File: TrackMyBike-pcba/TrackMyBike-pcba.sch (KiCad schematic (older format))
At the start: 3 parts

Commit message: Add project description
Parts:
- gave numbers to parts that had none: 1
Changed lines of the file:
@@
 $EndSheet
 $Comp
-L Connector_Generic:Conn_01x02 J?
+L Connector_Generic:Conn_01x02 J
 U 1 1 5F18731B
 P 8900 1150
-F 0 "J?" H 8980 1142 50  0000 L CNN
+F 0 "J" H 8980 1142 50  0000 L CNN
 F 1 "Conn_01x02" H 8980 1051 50  0000 L CNN
 F 2 "" H 8900 1150 50  0001 C CNN
@@
 $EndComp
 $Comp
-L Connector_Generic:Conn_01x02 J?
+L Connector_Generic:Conn_01x02 J
 U 1 1 5F187BB9
 P 10350 1150
-F 0 "J?" H 10430 1142 50  0000 L CNN
+F 0 "J" H 10430 1142 50  0000 L CNN
 F 1 "Conn_01x02" H 10430 1051 50  0000 L CNN
 F 2 "" H 10350 1150 50  0001 C CNN
@@
 $EndComp
 $Comp
-L power:+BATT #PWR?
+L power:+BATT #PWR
 U 1 1 5F1880E1
 P 8700 1150
-F 0 "#PWR?" H 8700 1000 50  0001 C CNN
+F 0 "#PWR" H 8700 1000 50  0001 C CNN
 F 1 "+BATT" H 8715 1323 50  0000 C CNN
 F 2 "" H 8700 1150 50  0001 C CNN
@@
 $EndComp
 $Comp
-L power:GND #PWR?
+L power:GND #PWR
 U 1 1 5F188BA8
 P 8700 1250
-F 0 "#PWR?" H 8700 1000 50  0001 C CNN
+F 0 "#PWR" H 8700 1000 50  0001 C CNN
 F 1 "GND" H 8705 1077 50  0000 C CNN
 F 2 "" H 8700 1250 50  0001 C CNN
@@
 $EndComp
 $Comp
-L power:GND #PWR?
+L power:GND #PWR
 U 1 1 5F188E4C
 P 10150 1250
-F 0 "#PWR?" H 10150 1000 50  0001 C CNN
+F 0 "#PWR" H 10150 1000 50  0001 C CNN
 F 1 "GND" H 10155 1077 50  0000 C CNN
 F 2 "" H 10150 1250 50  0001 C CNN
@@
 $EndComp
 $Comp
-L power:VSOLAR #PWR?
+L power:VSOLAR #PWR
 U 1 1 5F18A31C
 P 10150 1150
-F 0 "#PWR?" H 10150 1000 50  0001 C CNN
+F 0 "#PWR" H 10150 1000 50  0001 C CNN
 F 1 "VSOLAR" H 10165 1323 50  0000 C CNN
 F 2 "" H 10150 1150 50  0001 C CNN
@@
 $EndSheet
 $Comp
-L Connector:USB_B_Micro J?
+L Connector:USB_B_Micro J
 U 1 1 5F19E94A
 P 8850 2100
-F 0 "J?" H 8907 2567 50  0000 C CNN
+F 0 "J" H 8907 2567 50  0000 C CNN
 F 1 "USB_B_Micro" H 8907 2476 50  0000 C CNN
 F 2 "" H 9000 2050 50  0001 C CNN
@@
 NoConn ~ 9150 2300
 $Comp
-L power:GND #PWR?
+L power:GND #PWR
 U 1 1 5F19E955
 P 8750 2600
-F 0 "#PWR?" H 8750 2350 50  0001 C CNN
+F 0 "#PWR" H 8750 2350 50  0001 C CNN
 F 1 "GND" H 8755 2427 50  0000 C CNN
 F 2 "" H 8750 2600 50  0001 C CNN
@@
 	8750 2550 8750 2600
 $Comp
-L power:VBUS #PWR?
+L power:VBUS #PWR
 U 1 1 5F19EF28
 P 9400 1900
-F 0 "#PWR?" H 9400 1750 50  0001 C CNN
+F 0 "#PWR" H 9400 1750 50  0001 C CNN
 F 1 "VBUS" H 9415 2073 50  0000 C CNN
 F 2 "" H 9400 1900 50  0001 C CNN

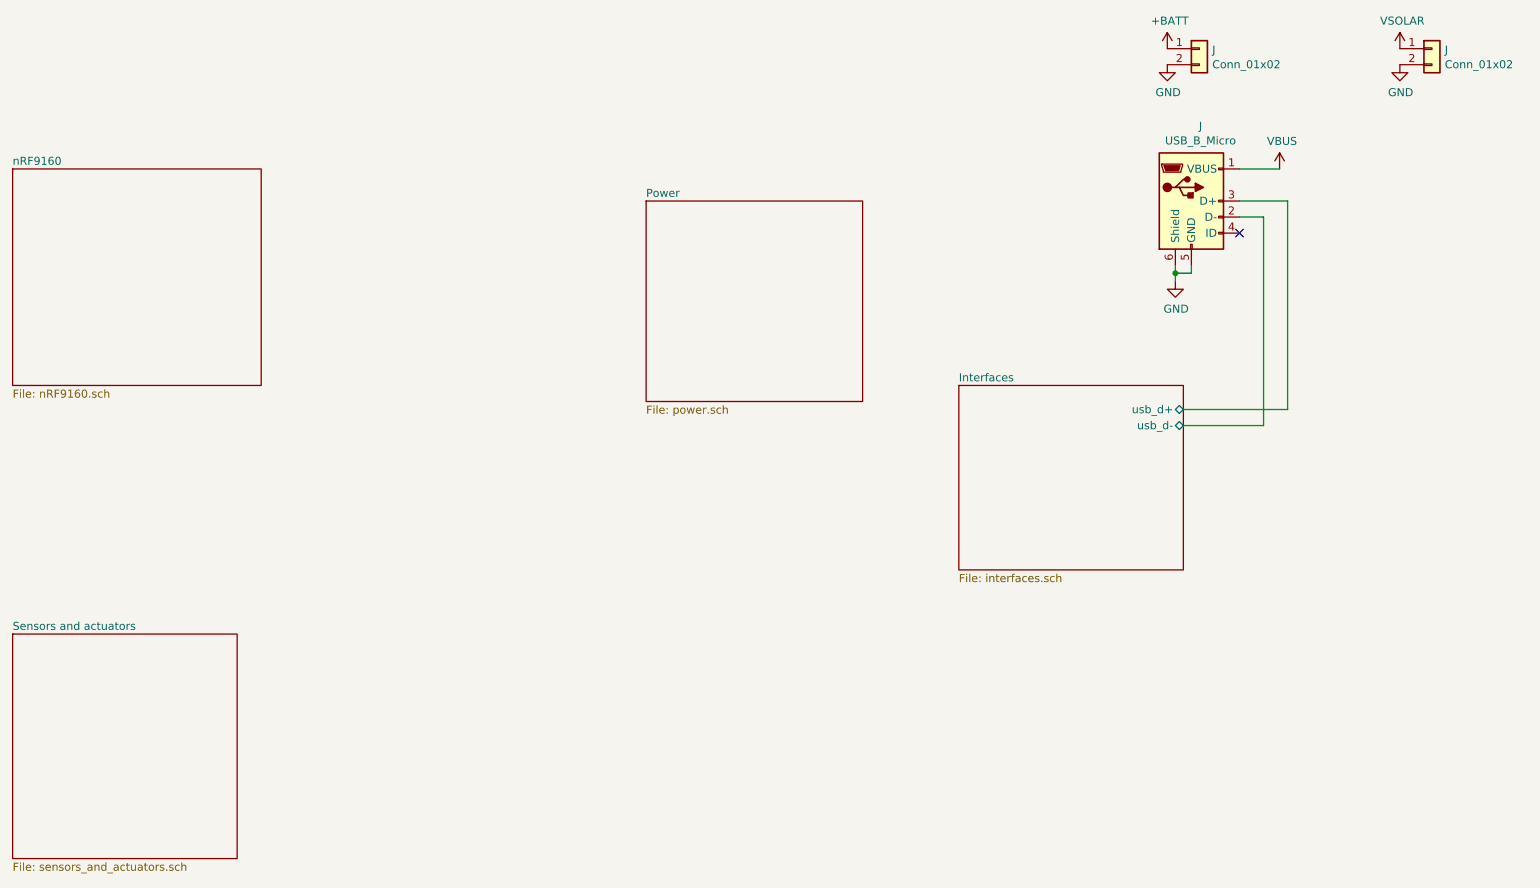
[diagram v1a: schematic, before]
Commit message: Add SIM card, FTDI IC
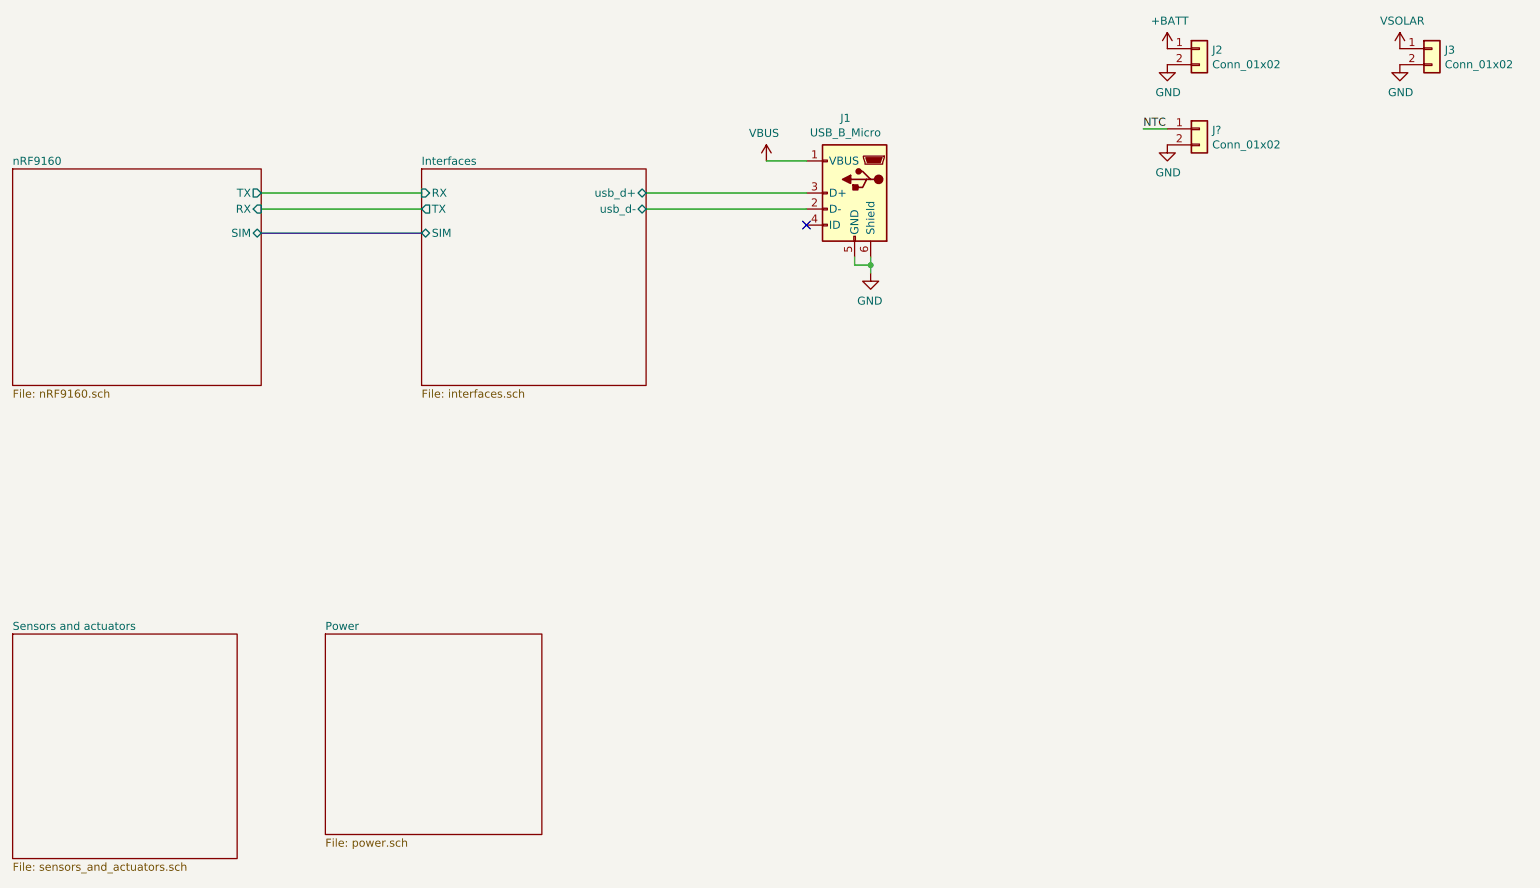
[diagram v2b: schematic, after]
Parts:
- added J?: Conn_01x02, symbol Connector_Generic:Conn_01x02
- renumbered J to J1, J to J2, J to J3
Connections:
- net GND: now also J?.2 (Pin_2)
- new net NTC: J?.1 (Pin_1)
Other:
- moved on the sheet: J1
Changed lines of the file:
@@
 F0 "nRF9160" 50
 F1 "nRF9160.sch" 50
+F2 "SIM" B R 3050 2300 50
+F3 "RX" I R 3050 2150 50
+F4 "TX" O R 3050 2050 50
 $EndSheet
 $Sheet
-S 5450 2100 1350 1250
+S 3450 4800 1350 1250
 U 5F16A6AE
 F0 "Power" 50
 F1 "power.sch" 50
 $EndSheet
+$Sheet
+S 1500 4800 1400 1400
+U 5F18B9BE
+F0 "Sensors and actuators" 50
+F1 "sensors_and_actuators.sch" 50
+$EndSheet
+$Sheet
+S 4050 1900 1400 1350
+U 5F19B71B
+F0 "Interfaces" 50
+F1 "interfaces.sch" 50
+F2 "usb_d+" B R 5450 2050 50
+F3 "usb_d-" B R 5450 2150 50
+F4 "RX" I L 4050 2050 50
+F5 "TX" O L 4050 2150 50
+F6 "SIM" B L 4050 2300 50
+$EndSheet
 $Comp
-L Connector_Generic:Conn_01x02 J
-U 1 1 5F18731B
-P 8900 1150
-F 0 "J" H 8980 1142 50  0000 L CNN
-F 1 "Conn_01x02" H 8980 1051 50  0000 L CNN
-F 2 "" H 8900 1150 50  0001 C CNN
-F 3 "~" H 8900 1150 50  0001 C CNN
-	1    8900 1150
+L power:VSOLAR #PWR0101
+U 1 1 5F18A31C
+P 10150 1150
+F 0 "#PWR0101" H 10150 1000 50  0001 C CNN
+F 1 "VSOLAR" H 10165 1323 50  0000 C CNN
+F 2 "" H 10150 1150 50  0001 C CNN
+F 3 "" H 10150 1150 50  0001 C CNN
+	1    10150 1150
 	1    0    0    -1
 $EndComp
 $Comp
-L Connector_Generic:Conn_01x02 J
+L power:GND #PWR0102
+U 1 1 5F188E4C
+P 10150 1250
+F 0 "#PWR0102" H 10150 1000 50  0001 C CNN
+F 1 "GND" H 10155 1077 50  0000 C CNN
+F 2 "" H 10150 1250 50  0001 C CNN
+F 3 "" H 10150 1250 50  0001 C CNN
+	1    10150 1250
+	1    0    0    -1
+$EndComp
+$Comp
+L power:GND #PWR0103
+U 1 1 5F188BA8
+P 8700 1250
+F 0 "#PWR0103" H 8700 1000 50  0001 C CNN
+F 1 "GND" H 8705 1077 50  0000 C CNN
+F 2 "" H 8700 1250 50  0001 C CNN
+F 3 "" H 8700 1250 50  0001 C CNN
+	1    8700 1250
+	1    0    0    -1
+$EndComp
+$Comp
+L power:+BATT #PWR0104
+U 1 1 5F1880E1
+P 8700 1150
+F 0 "#PWR0104" H 8700 1000 50  0001 C CNN
+F 1 "+BATT" H 8715 1323 50  0000 C CNN
+F 2 "" H 8700 1150 50  0001 C CNN
+F 3 "" H 8700 1150 50  0001 C CNN
+	1    8700 1150
+	1    0    0    -1
+$EndComp
+$Comp
+L Connector_Generic:Conn_01x02 J3
 U 1 1 5F187BB9
 P 10350 1150
-F 0 "J" H 10430 1142 50  0000 L CNN
+F 0 "J3" H 10430 1142 50  0000 L CNN
 F 1 "Conn_01x02" H 10430 1051 50  0000 L CNN
 F 2 "" H 10350 1150 50  0001 C CNN
@@
 $EndComp
 $Comp
-L power:+BATT #PWR
-U 1 1 5F1880E1
-P 8700 1150
-F 0 "#PWR" H 8700 1000 50  0001 C CNN
-F 1 "+BATT" H 8715 1323 50  0000 C CNN
-F 2 "" H 8700 1150 50  0001 C CNN
-F 3 "" H 8700 1150 50  0001 C CNN
-	1    8700 1150
+L Connector_Generic:Conn_01x02 J2
+U 1 1 5F18731B
+P 8900 1150
+F 0 "J2" H 8980 1142 50  0000 L CNN
+F 1 "Conn_01x02" H 8980 1051 50  0000 L CNN
+F 2 "" H 8900 1150 50  0001 C CNN
+F 3 "~" H 8900 1150 50  0001 C CNN
+	1    8900 1150
+	1    0    0    -1
+$EndComp
+Wire Wire Line
+	5450 2150 6450 2150
+Wire Wire Line
+	5450 2050 6450 2050
+Wire Wire Line
+	6450 1850 6200 1850
+$Comp
+L power:VBUS #PWR0105
+U 1 1 5F19EF28
+P 6200 1850
+F 0 "#PWR0105" H 6200 1700 50  0001 C CNN
+F 1 "VBUS" H 6215 2023 50  0000 C CNN
+F 2 "" H 6200 1850 50  0001 C CNN
+F 3 "" H 6200 1850 50  0001 C CNN
+	1    6200 1850
+	-1   0    0    -1
+$EndComp
+Wire Wire Line
+	6850 2500 6850 2550
+Connection ~ 6850 2500
+Wire Wire Line
+	6750 2500 6750 2450
+Wire Wire Line
+	6850 2500 6750 2500
+Wire Wire Line
+	6850 2450 6850 2500
+$Comp
+L power:GND #PWR0106
+U 1 1 5F19E955
+P 6850 2550
+F 0 "#PWR0106" H 6850 2300 50  0001 C CNN
+F 1 "GND" H 6855 2377 50  0000 C CNN
+F 2 "" H 6850 2550 50  0001 C CNN
+F 3 "" H 6850 2550 50  0001 C CNN
+	1    6850 2550
+	-1   0    0    -1
+$EndComp
+NoConn ~ 6450 2250
+$Comp
+L Connector:USB_B_Micro J1
+U 1 1 5F19E94A
+P 6750 2050
+F 0 "J1" H 6807 2517 50  0000 C CNN
+F 1 "USB_B_Micro" H 6807 2426 50  0000 C CNN
+F 2 "" H 6900 2000 50  0001 C CNN
+F 3 "~" H 6900 2000 50  0001 C CNN
+	1    6750 2050
+	-1   0    0    -1
+$EndComp
+Wire Bus Line
+	3050 2300 4050 2300
+Wire Wire Line
+	3050 2150 4050 2150
+Wire Wire Line
+	4050 2050 3050 2050
+$Comp
+L power:GND #PWR?
+U 1 1 5F1C3374
+P 8700 1750
+F 0 "#PWR?" H 8700 1500 50  0001 C CNN
+F 1 "GND" H 8705 1577 50  0000 C CNN
+F 2 "" H 8700 1750 50  0001 C CNN
+F 3 "" H 8700 1750 50  0001 C CNN
+	1    8700 1750
 	1    0    0    -1
 $EndComp
 $Comp
-L power:GND #PWR
-U 1 1 5F188BA8
-P 8700 1250
-F 0 "#PWR" H 8700 1000 50  0001 C CNN
-F 1 "GND" H 8705 1077 50  0000 C CNN
-F 2 "" H 8700 1250 50  0001 C CNN
-F 3 "" H 8700 1250 50  0001 C CNN
-	1    8700 1250
+L Connector_Generic:Conn_01x02 J?
+U 1 1 5F1C3380
+P 8900 1650
+F 0 "J?" H 8980 1642 50  0000 L CNN
+F 1 "Conn_01x02" H 8980 1551 50  0000 L CNN
+F 2 "" H 8900 1650 50  0001 C CNN
+F 3 "~" H 8900 1650 50  0001 C CNN
+	1    8900 1650
 	1    0    0    -1
 $EndComp
-$Comp
-L power:GND #PWR
-U 1 1 5F188E4C
-P 10150 1250
-F 0 "#PWR" H 10150 1000 50  0001 C CNN
-F 1 "GND" H 10155 1077 50  0000 C CNN
-F 2 "" H 10150 1250 50  0001 C CNN
-F 3 "" H 10150 1250 50  0001 C CNN
-	1    10150 1250
-	1    0    0    -1
-$EndComp
-$Comp
-L power:VSOLAR #PWR
-U 1 1 5F18A31C
-P 10150 1150
-F 0 "#PWR" H 10150 1000 50  0001 C CNN
-F 1 "VSOLAR" H 10165 1323 50  0000 C CNN
-F 2 "" H 10150 1150 50  0001 C CNN
-F 3 "" H 10150 1150 50  0001 C CNN
-	1    10150 1150
-	1    0    0    -1
-$EndComp
-$Sheet
-S 1500 4800 1400 1400
-U 5F18B9BE
-F0 "Sensors and actuators" 50
-F1 "sensors_and_actuators.sch" 50
-$EndSheet
-$Sheet
-S 7400 3250 1400 1150
-U 5F19B71B
-F0 "Interfaces" 50
-F1 "interfaces.sch" 50
-F2 "usb_d+" B R 8800 3400 50
-F3 "usb_d-" B R 8800 3500 50
-$EndSheet
-$Comp
-L Connector:USB_B_Micro J
-U 1 1 5F19E94A
-P 8850 2100
-F 0 "J" H 8907 2567 50  0000 C CNN
-F 1 "USB_B_Micro" H 8907 2476 50  0000 C CNN
-F 2 "" H 9000 2050 50  0001 C CNN
-F 3 "~" H 9000 2050 50  0001 C CNN
-	1    8850 2100
-	1    0    0    -1
-$EndComp
-NoConn ~ 9150 2300
-$Comp
-L power:GND #PWR
-U 1 1 5F19E955
-P 8750 2600
-F 0 "#PWR" H 8750 2350 50  0001 C CNN
-F 1 "GND" H 8755 2427 50  0000 C CNN
-F 2 "" H 8750 2600 50  0001 C CNN
-F 3 "" H 8750 2600 50  0001 C CNN
-	1    8750 2600
-	1    0    0    -1
-$EndComp
+Text Label 8550 1650 0    50   ~ 0
+NTC
 Wire Wire Line
-	8750 2500 8750 2550
-Wire Wire Line
-	8750 2550 8850 2550
-Wire Wire Line
-	8850 2550 8850 2500
-Connection ~ 8750 2550
-Wire Wire Line
-	8750 2550 8750 2600
-$Comp
-L power:VBUS #PWR
-U 1 1 5F19EF28
-P 9400 1900
-F 0 "#PWR" H 9400 1750 50  0001 C CNN
-F 1 "VBUS" H 9415 2073 50  0000 C CNN
-F 2 "" H 9400 1900 50  0001 C CNN
-F 3 "" H 9400 1900 50  0001 C CNN
-	1    9400 1900
-	1    0    0    -1
-$EndComp
-Wire Wire Line
-	9150 1900 9400 1900
-Wire Wire Line
-	8800 3500 9300 3500
-Wire Wire Line
-	9300 3500 9300 2200
-Wire Wire Line
-	9300 2200 9150 2200
-Wire Wire Line
-	8800 3400 9450 3400
-Wire Wire Line
-	9450 3400 9450 2100
-Wire Wire Line
-	9450 2100 9150 2100
+	8550 1650 8700 1650
 $EndSCHEMATC

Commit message: Add power schematic
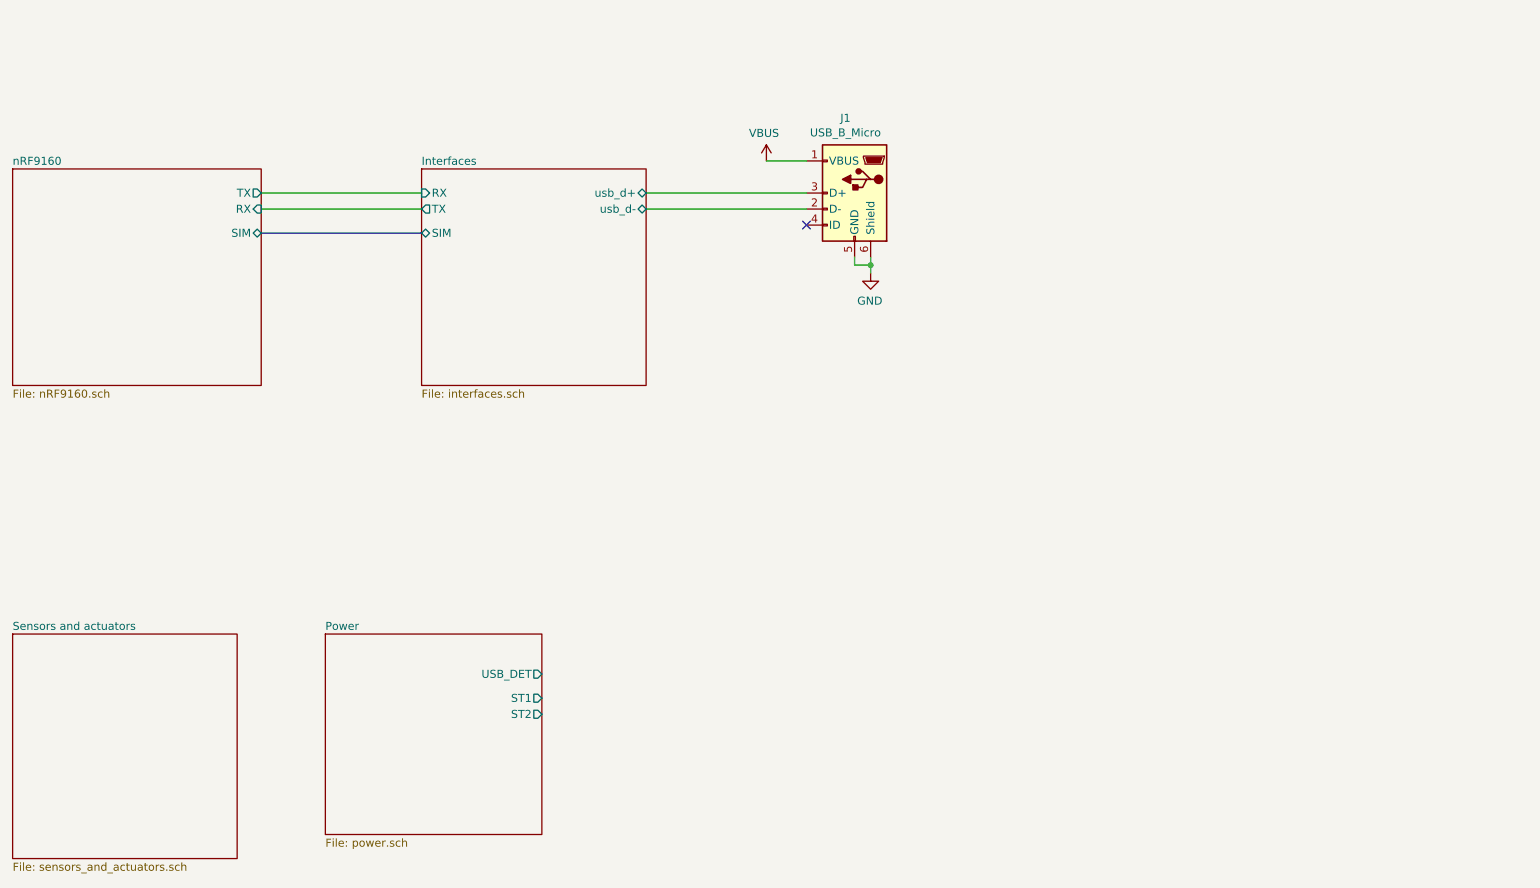
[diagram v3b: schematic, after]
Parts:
- removed J2, J3, J?: Conn_01x02, symbol Connector_Generic:Conn_01x02
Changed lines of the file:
@@
 F0 "Power" 50
 F1 "power.sch" 50
+F2 "ST1" O R 4800 5200 50
+F3 "USB_DET" O R 4800 5050 50
+F4 "ST2" O R 4800 5300 50
 $EndSheet
 $Sheet
@@
 F6 "SIM" B L 4050 2300 50
 $EndSheet
-$Comp
-L power:VSOLAR #PWR0101
-U 1 1 5F18A31C
-P 10150 1150
-F 0 "#PWR0101" H 10150 1000 50  0001 C CNN
-F 1 "VSOLAR" H 10165 1323 50  0000 C CNN
-F 2 "" H 10150 1150 50  0001 C CNN
-F 3 "" H 10150 1150 50  0001 C CNN
-	1    10150 1150
-	1    0    0    -1
-$EndComp
-$Comp
-L power:GND #PWR0102
-U 1 1 5F188E4C
-P 10150 1250
-F 0 "#PWR0102" H 10150 1000 50  0001 C CNN
-F 1 "GND" H 10155 1077 50  0000 C CNN
-F 2 "" H 10150 1250 50  0001 C CNN
-F 3 "" H 10150 1250 50  0001 C CNN
-	1    10150 1250
-	1    0    0    -1
-$EndComp
-$Comp
-L power:GND #PWR0103
-U 1 1 5F188BA8
-P 8700 1250
-F 0 "#PWR0103" H 8700 1000 50  0001 C CNN
-F 1 "GND" H 8705 1077 50  0000 C CNN
-F 2 "" H 8700 1250 50  0001 C CNN
-F 3 "" H 8700 1250 50  0001 C CNN
-	1    8700 1250
-	1    0    0    -1
-$EndComp
-$Comp
-L power:+BATT #PWR0104
-U 1 1 5F1880E1
-P 8700 1150
-F 0 "#PWR0104" H 8700 1000 50  0001 C CNN
-F 1 "+BATT" H 8715 1323 50  0000 C CNN
-F 2 "" H 8700 1150 50  0001 C CNN
-F 3 "" H 8700 1150 50  0001 C CNN
-	1    8700 1150
-	1    0    0    -1
-$EndComp
-$Comp
-L Connector_Generic:Conn_01x02 J3
-U 1 1 5F187BB9
-P 10350 1150
-F 0 "J3" H 10430 1142 50  0000 L CNN
-F 1 "Conn_01x02" H 10430 1051 50  0000 L CNN
-F 2 "" H 10350 1150 50  0001 C CNN
-F 3 "~" H 10350 1150 50  0001 C CNN
-	1    10350 1150
-	1    0    0    -1
-$EndComp
-$Comp
-L Connector_Generic:Conn_01x02 J2
-U 1 1 5F18731B
-P 8900 1150
-F 0 "J2" H 8980 1142 50  0000 L CNN
-F 1 "Conn_01x02" H 8980 1051 50  0000 L CNN
-F 2 "" H 8900 1150 50  0001 C CNN
-F 3 "~" H 8900 1150 50  0001 C CNN
-	1    8900 1150
-	1    0    0    -1
-$EndComp
 Wire Wire Line
 	5450 2150 6450 2150
@@
 Wire Wire Line
 	4050 2050 3050 2050
-$Comp
-L power:GND #PWR?
-U 1 1 5F1C3374
-P 8700 1750
-F 0 "#PWR?" H 8700 1500 50  0001 C CNN
-F 1 "GND" H 8705 1577 50  0000 C CNN
-F 2 "" H 8700 1750 50  0001 C CNN
-F 3 "" H 8700 1750 50  0001 C CNN
-	1    8700 1750
-	1    0    0    -1
-$EndComp
-$Comp
-L Connector_Generic:Conn_01x02 J?
-U 1 1 5F1C3380
-P 8900 1650
-F 0 "J?" H 8980 1642 50  0000 L CNN
-F 1 "Conn_01x02" H 8980 1551 50  0000 L CNN
-F 2 "" H 8900 1650 50  0001 C CNN
-F 3 "~" H 8900 1650 50  0001 C CNN
-	1    8900 1650
-	1    0    0    -1
-$EndComp
-Text Label 8550 1650 0    50   ~ 0
-NTC
-Wire Wire Line
-	8550 1650 8700 1650
 $EndSCHEMATC

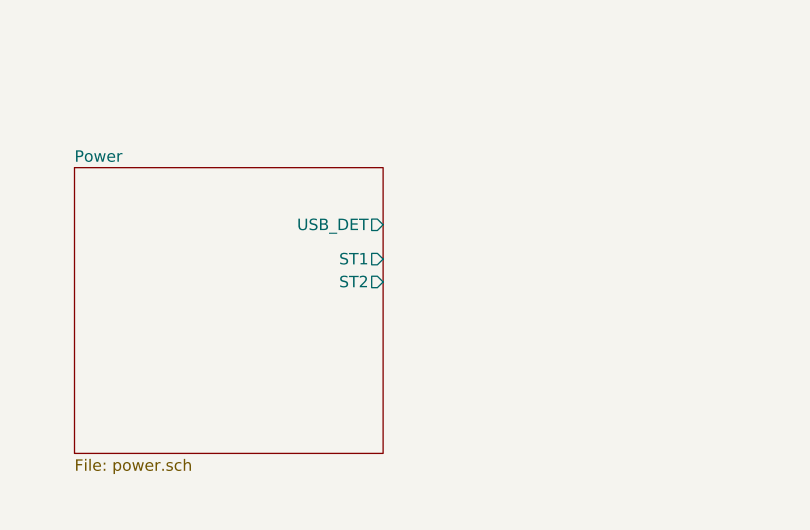
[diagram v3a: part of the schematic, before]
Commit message: Add buck-boost converter to regulate VBAT to 3V3
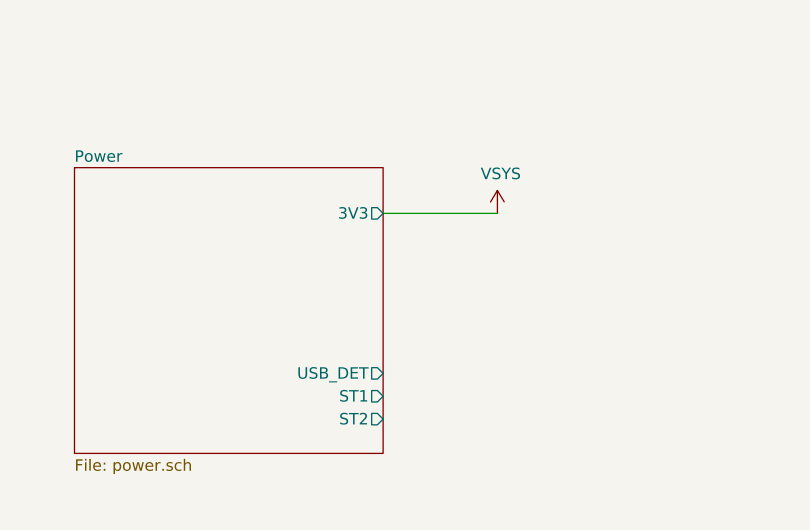
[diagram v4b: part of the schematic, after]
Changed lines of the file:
@@
 F0 "Power" 50
 F1 "power.sch" 50
-F2 "ST1" O R 4800 5200 50
-F3 "USB_DET" O R 4800 5050 50
-F4 "ST2" O R 4800 5300 50
+F2 "ST1" O R 4800 5800 50
+F3 "USB_DET" O R 4800 5700 50
+F4 "ST2" O R 4800 5900 50
+F5 "3V3" O R 4800 5000 50
 $EndSheet
 $Sheet
@@
 Wire Wire Line
 	4050 2050 3050 2050
+Wire Wire Line
+	4800 5000 5300 5000
+$Comp
+L power:VSYS #PWR?
+U 1 1 5F3FA9BA
+P 5300 5000
+F 0 "#PWR?" H 5300 4850 50  0001 C CNN
+F 1 "VSYS" H 5315 5173 50  0000 C CNN
+F 2 "" H 5300 5000 50  0001 C CNN
+F 3 "" H 5300 5000 50  0001 C CNN
+	1    5300 5000
+	1    0    0    -1
+$EndComp
 $EndSCHEMATC
